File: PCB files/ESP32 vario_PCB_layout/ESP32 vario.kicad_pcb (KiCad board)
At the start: 2 copper layers, 40 x 67.5 mm, 9 parts, among them U2 ESP32-S3 Waveshare

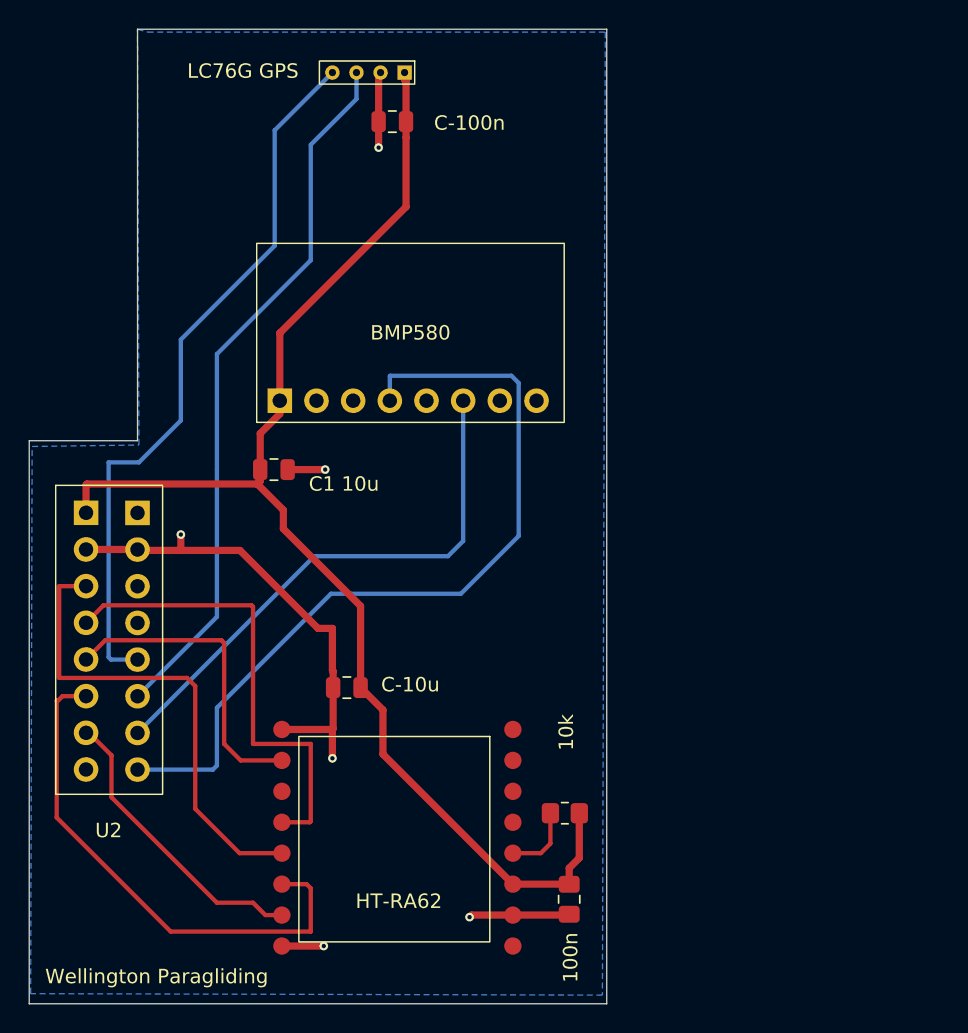
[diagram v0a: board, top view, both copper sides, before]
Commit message: New PCB Layout
Fully rebuilt PCB from scratch, LoRa module is now compatible with FANET, Key button to be moved to BOOT key. More work to do.
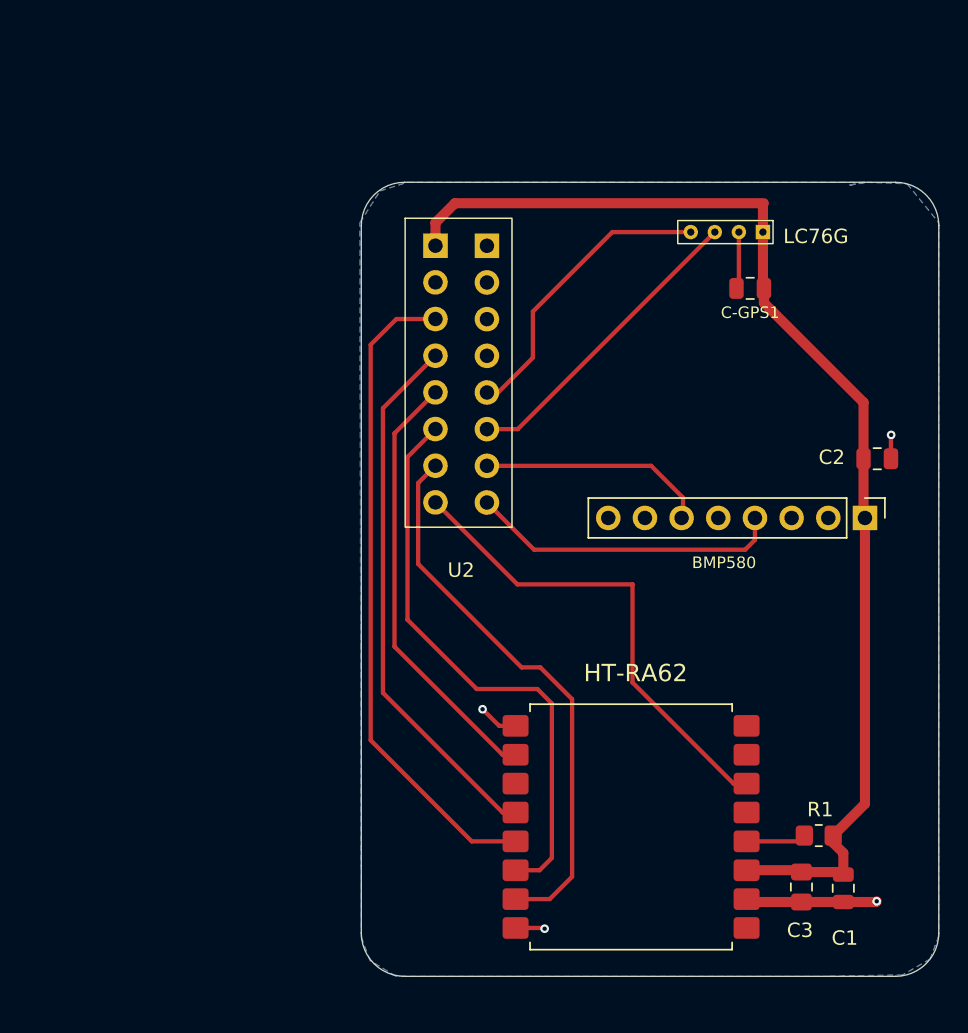
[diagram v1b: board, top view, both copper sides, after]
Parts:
- removed 100n: 100n, Capacitor_SMD:C_0805_2012Metric_Pad1.18x1.45mm_HandSolder
- removed 10k: 10K, Resistor_SMD:R_0805_2012Metric_Pad1.20x1.40mm_HandSolder
- removed C-100n: 100n, Capacitor_SMD:C_0805_2012Metric
- removed C-10u: 10u, Capacitor_SMD:C_0805_2012Metric
- removed C1 10u: 10u, Capacitor_SMD:C_0805_2012Metric
- removed LC76G GPS: LC76G GPS, Flight cumputer footprints:LC76G- 4 pin
- added C-GPS1: 100n, Capacitor_SMD:C_0805_2012Metric, F.Cu at (159.9, 85.5)
- added C1: 10u, Capacitor_SMD:C_0805_2012Metric, F.Cu at (166.4, 127.0)
- added C2: 10u, Capacitor_SMD:C_0805_2012Metric, F.Cu at (168.7, 97.2)
- added C3: 100n, Capacitor_SMD:C_0805_2012Metric_Pad1.18x1.45mm_HandSolder, F.Cu at (163.5, 126.9)
- added LC76G: LC76G GPS, Flight cumputer footprints:LC76G- 4 pin, F.Cu at (160.8, 81.5)
- added R1: 10K, Resistor_SMD:R_0805_2012Metric_Pad1.20x1.40mm_HandSolder, F.Cu at (164.7, 123.3)
- BMP580: footprint Flight cumputer footprints:BMP580 Header -> Connector_PinHeader_2.54mm:PinHeader_1x08_P2.54mm_Vertical
- HT-RA62: footprint Flight cumputer footprints:HT-RA62 -> NiceNano-Everything:HT-RA62
- moved BMP580 41.3 mm to (167.9, 101.3), turned to -90 degrees
- moved U2 30.5 mm to (138.1, 82.5)
- moved HT-RA62 16.2 mm to (151.7, 122.8), turned to 180 degrees
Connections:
- HT-RA62 pad 6: unconnected-(U1-DIO1-Pad6) -> DIO1
- U2 pad 8: unconnected-(U2-GP18-Pad8) -> DIO1
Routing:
- net SCL: track 56.9 -> 21.7 mm
- net DIO1: track 0.00 -> 33.6 mm
- net GND: track 50.7 -> 19.5 mm, vias 6 -> 4
- net Tx: track 50.2 -> 20.6 mm
- net Rx: track 49.5 -> 21.4 mm
- net SDA: track 37.8 -> 15.9 mm
- net NSS(CS): track 21.0 -> 38.7 mm
- net MISO: track 33.7 -> 45.6 mm
- net BUSY: track 21.7 -> 30.3 mm
- net +3V: track 90.8 -> 82.4 mm
- net SCK: track 33.0 -> 37.5 mm
- net MOSI: track 36.3 -> 40.0 mm
- net RST: track 4.98 -> 4.17 mm
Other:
- board size 40 x 67.5 mm -> 40 x 55 mm
- board text removed: "Wellington Paragliding"

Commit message: Removed DIO18 as it conflicts with Key pin
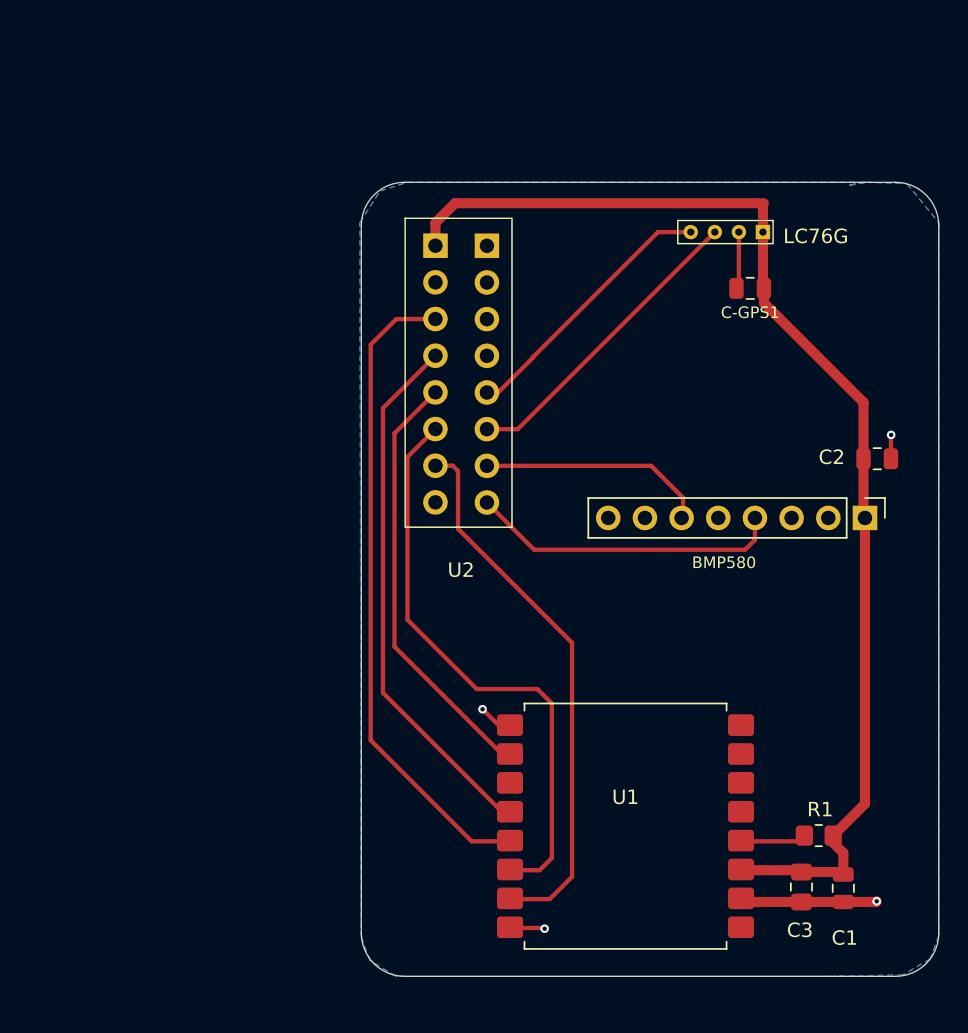
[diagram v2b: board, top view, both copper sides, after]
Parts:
- removed HT-RA62: HT-RA62, NiceNano-Everything:HT-RA62
- added U1: HT-RA62, NiceNano-Everything:HT-RA62, F.Cu at (151.3, 122.7)
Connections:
- U2 pad 8: DIO1 -> unconnected-(U2-GP18-Pad8)
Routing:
- net DIO1: track 33.6 -> 0.00 mm
- net Tx: track 20.6 -> 18.7 mm
- net NSS(CS): track 38.7 -> 37.6 mm
- net unconnected-(U1-DIO1-Pad6): track 0.00 -> 0.90 mm

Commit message: Added FANET
PCB has been rebuilt, FANET test code has been written, now need to go do some real world testing. Still more menu changes to be made.
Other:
- board text added: "A SARGENT"

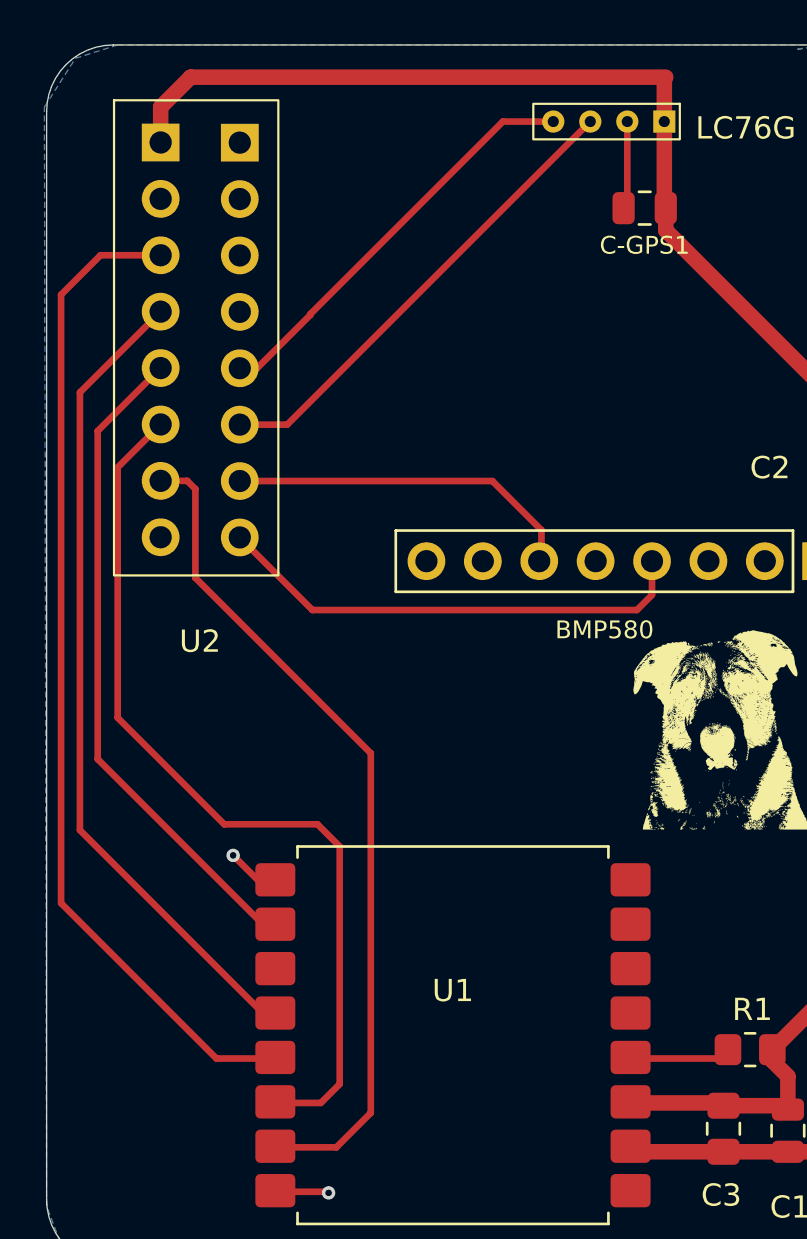
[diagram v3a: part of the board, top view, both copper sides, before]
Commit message: Fixed the header pins on the PCB
Header pins have been moved closer by 1mm, should make it easier to solder.
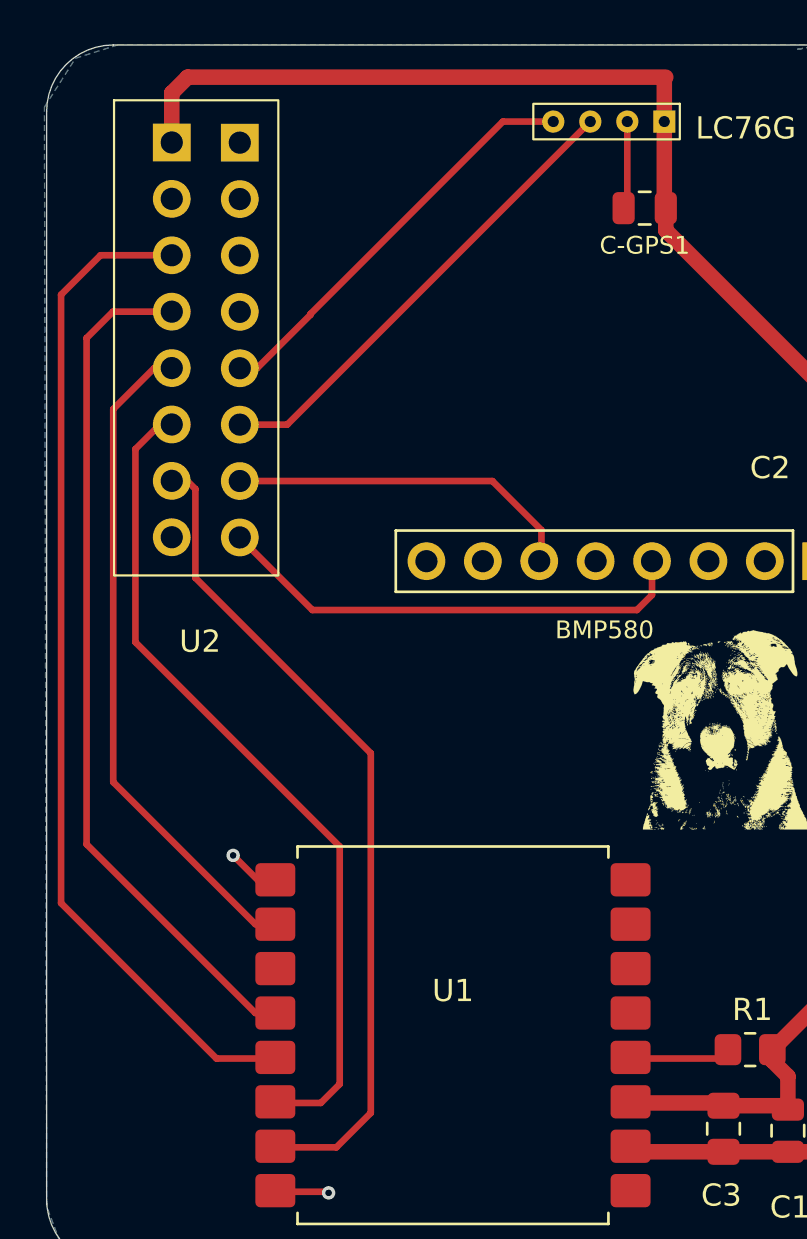
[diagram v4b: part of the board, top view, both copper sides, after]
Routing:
- net MOSI: track 40.0 -> 37.4 mm
- net SCK: track 37.5 -> 39.7 mm
- net BUSY: track 30.3 -> 31.1 mm
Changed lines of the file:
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@@
 		(sheetname "/")
 		(sheetfile "ESP32 vario.kicad_sch")
-		(units
-			(unit
-				(name "A")
-				(pins "1" "2" "3" "4" "5" "6" "7" "8" "9" "10" "11" "12" "13" "14" "15"
-					"16"
-				)
-			)
-		)
 		(attr through_hole)
 		(duplicate_pad_numbers_are_jumpers no)
@@
 		)
 		(pad "1" thru_hole rect
-			(at 0 0)
+			(at 0.5 0)
 			(size 1.7 1.7)
 			(drill 1)
@@
 		)
 		(pad "2" thru_hole circle
-			(at 0 2.54)
+			(at 0.5 2.54)
 			(size 1.7 1.7)
 			(drill 1)
@@
 		)
 		(pad "3" thru_hole circle
-			(at 0 5.08)
+			(at 0.5 5.08)
 			(size 1.7 1.7)
 			(drill 1)
@@
 		)
 		(pad "4" thru_hole circle
-			(at 0 7.62)
+			(at 0.5 7.62)
 			(size 1.7 1.7)
 			(drill 1)
@@
 		)
 		(pad "5" thru_hole circle
-			(at 0 10.16)
+			(at 0.5 10.16)
 			(size 1.7 1.7)
 			(drill 1)
@@
 		)
 		(pad "6" thru_hole circle
-			(at 0 12.7)
+			(at 0.5 12.7)
 			(size 1.7 1.7)
 			(drill 1)
@@
 		)
 		(pad "7" thru_hole circle
-			(at 0 15.24)
+			(at 0.5 15.24)
 			(size 1.7 1.7)
 			(drill 1)
@@
 		)
 		(pad "8" thru_hole circle
-			(at 0 17.78)
+			(at 0.5 17.78)
 			(size 1.7 1.7)
 			(drill 1)
@@
 	)
 	(segment
-		(start 139.486 79.55)
-		(end 160.886 79.55)
+		(start 160.886 79.55)
+		(end 139.35 79.55)
+		(width 0.7)
+		(layer "F.Cu")
+		(net "+3V")
+	)
+	(segment
+		(start 138.636 80.264)
+		(end 138.636 82.492)
 		(width 0.7)
 		(layer "F.Cu")
@@
 	)
 	(segment
-		(start 167.786 101.09)
-		(end 168.046 101.35)
+		(start 139.35 79.55)
+		(end 138.636 80.264)
 		(width 0.7)
 		(layer "F.Cu")
@@
 	)
 	(segment
-		(start 138.136 80.9)
-		(end 139.486 79.55)
+		(start 167.786 101.09)
+		(end 168.046 101.35)
 		(width 0.7)
 		(layer "F.Cu")
@@
 	)
 	(segment
-		(start 138.136 82.492)
-		(end 138.136 80.9)
-		(width 0.7)
-		(layer "F.Cu")
-		(net "+3V")
-	)
-	(segment
 		(start 166.386 124.55)
 		(end 166.386 126.05)
@@
 	)
 	(segment
-		(start 134.5 93.748)
-		(end 134.5 113.464)
+		(start 135.988 90.112)
+		(end 134.8 91.3)
 		(width 0.3)
 		(layer "F.Cu")
@@
 	)
 	(segment
-		(start 138.136 90.112)
-		(end 134.5 93.748)
+		(start 134.8 91.3)
+		(end 134.8 114.1)
+		(width 0.3)
+		(layer "F.Cu")
+		(net "SCK")
+	)
+	(segment
+		(start 134.8 114.1)
+		(end 142.4 121.7)
+		(width 0.3)
+		(layer "F.Cu")
+		(net "SCK")
+	)
+	(segment
+		(start 142.4 121.7)
+		(end 143.3 121.7)
 		(width 0.3)
 		(layer "F.Cu")
@@
 	)
 	(segment
-		(start 134.5 113.464)
-		(end 142.786 121.75)
+		(start 138.636 90.112)
+		(end 135.988 90.112)
 		(width 0.3)
 		(layer "F.Cu")
@@
 	)
 	(segment
-		(start 142.786 117.75)
-		(end 135.3 110.264)
+		(start 138.636 92.652)
+		(end 137.848 92.652)
 		(width 0.3)
 		(layer "F.Cu")
@@
 	)
 	(segment
-		(start 143.686 117.75)
-		(end 142.786 117.75)
+		(start 137.848 92.652)
+		(end 136 94.5)
 		(width 0.3)
 		(layer "F.Cu")
@@
 	)
 	(segment
-		(start 135.3 110.264)
-		(end 135.3 95.488)
+		(start 136 111.3)
+		(end 142.4 117.7)
 		(width 0.3)
 		(layer "F.Cu")
@@
 	)
 	(segment
-		(start 135.3 95.488)
-		(end 138.136 92.652)
+		(start 136 94.5)
+		(end 136 111.3)
 		(width 0.3)
 		(layer "F.Cu")
@@
 	)
 	(segment
-		(start 141 113.2)
-		(end 145.2 113.2)
+		(start 143.686 117.75)
+		(end 142.786 117.75)
 		(width 0.3)
 		(layer "F.Cu")
-		(net "MOSI")
+		(net "BUSY")
 	)
 	(segment
-		(start 136.2 97.128)
-		(end 136.2 108.4)
+		(start 142.4 117.7)
+		(end 143.3 117.7)
 		(width 0.3)
 		(layer "F.Cu")
-		(net "MOSI")
+		(net "BUSY")
 	)
 	(segment
-		(start 136.2 108.4)
-		(end 141 113.2)
+		(start 138.108 95.192)
+		(end 138.636 95.192)
 		(width 0.3)
 		(layer "F.Cu")
@@
 	)
 	(segment
-		(start 145.35 125.75)
-		(end 143.686 125.75)
+		(start 137 105)
+		(end 137 96.3)
 		(width 0.3)
 		(layer "F.Cu")
@@
 	)
 	(segment
-		(start 146.2 124.9)
+		(start 143.686 125.75)
 		(end 145.35 125.75)
 		(width 0.3)
@@
 	)
 	(segment
-		(start 145.2 113.2)
-		(end 146.2 114.2)
+		(start 146.2 114.2)
+		(end 137 105)
 		(width 0.3)
 		(layer "F.Cu")
@@
 	)
 	(segment
-		(start 146.2 114.2)
+		(start 145.35 125.75)
 		(end 146.2 124.9)
 		(width 0.3)
@@
 	)
 	(segment
-		(start 138.136 95.192)
-		(end 136.2 97.128)
+		(start 146.2 124.9)
+		(end 146.2 114.2)
+		(width 0.3)
+		(layer "F.Cu")
+		(net "MOSI")
+	)
+	(segment
+		(start 137 96.3)
+		(end 138.108 95.192)
 		(width 0.3)
 		(layer "F.Cu")
